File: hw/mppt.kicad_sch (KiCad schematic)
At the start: 9 parts

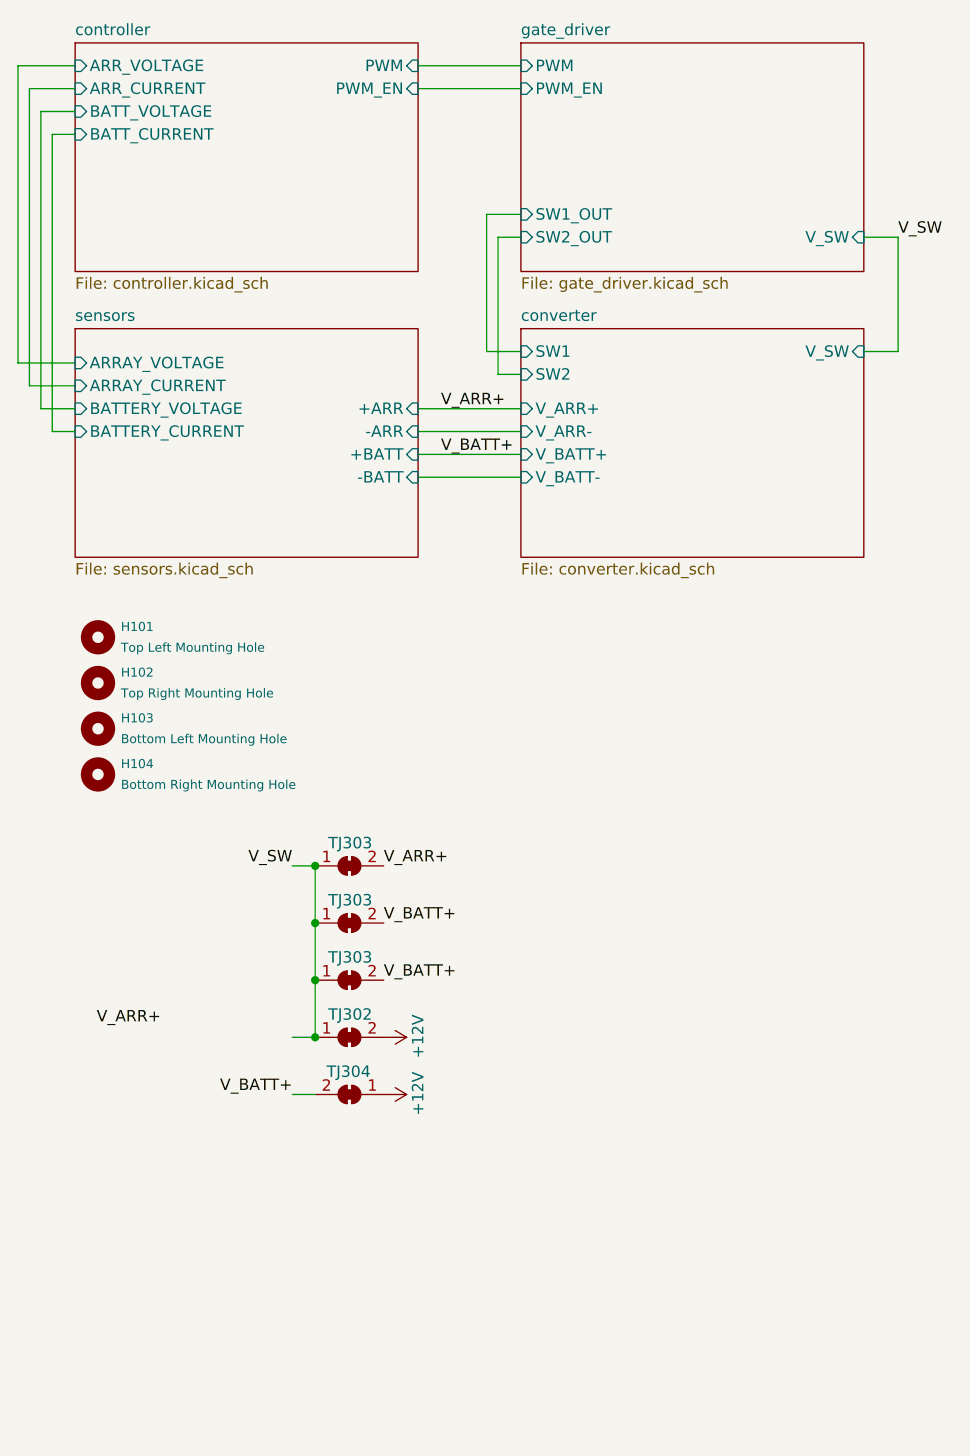
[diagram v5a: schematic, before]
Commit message: Added proper signal TPs for Vsw, both gate signals, and PWM, added BNC connector for PWM control signal to STM analog pin, increased Vsw zone on F.cu, in.1, and in.2, reduced vias directly under fets, changed heatsink holesto pads for proper zone margins
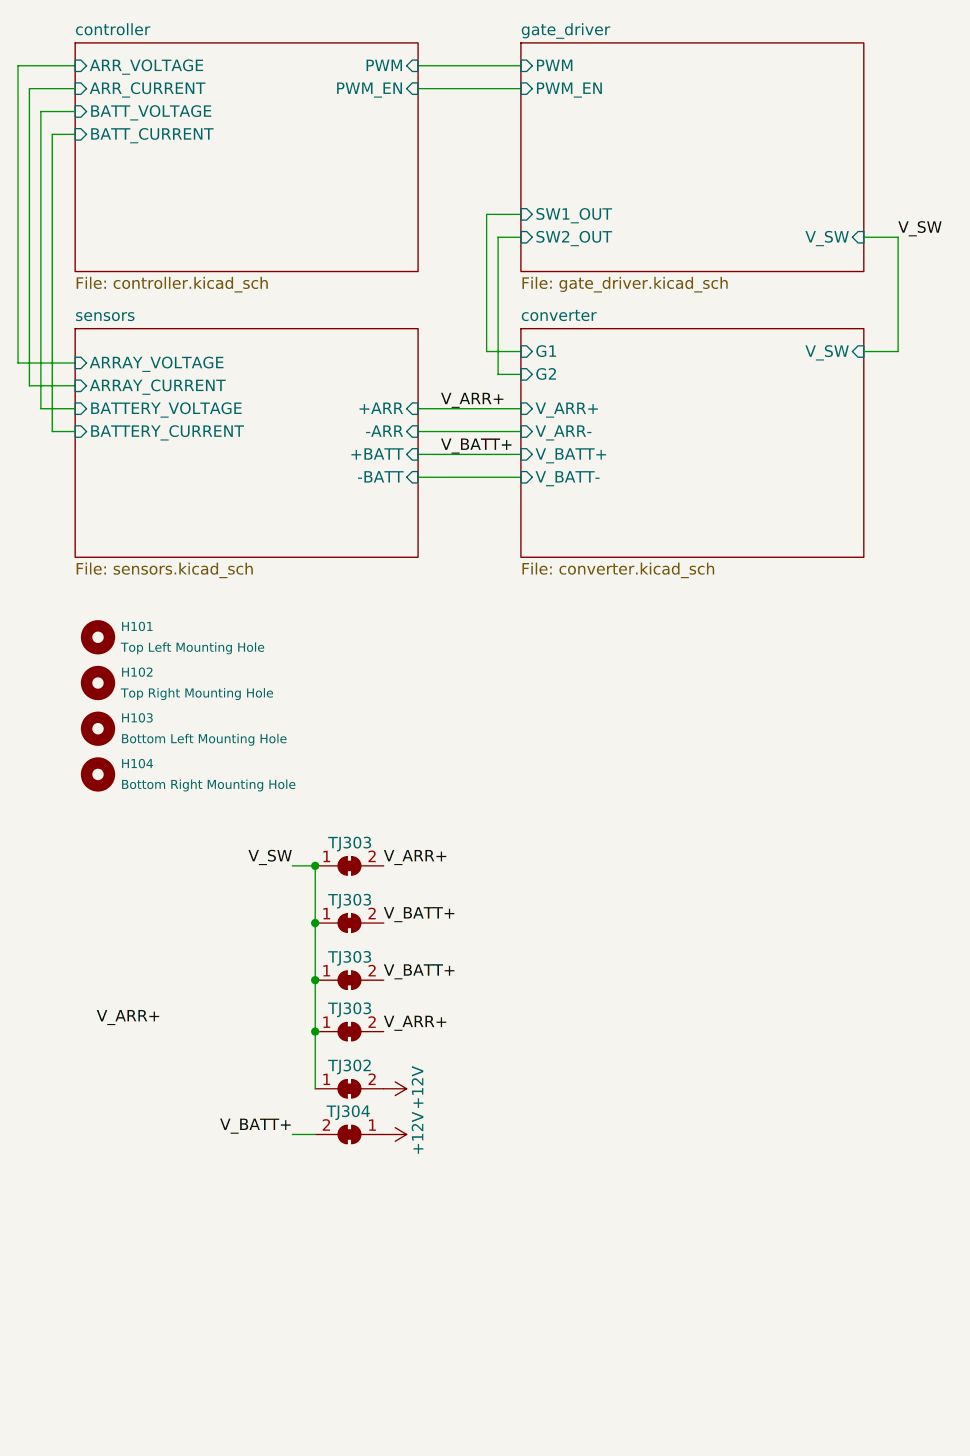
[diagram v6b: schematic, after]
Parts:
- added TJ303: Thermal Jumper, Resistor_SMD:R_0805_2012Metric, symbol Jumper:SolderJumper_2_Bridged
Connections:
- net V_ARR+: now also TJ303.2 (B)
- net V_SW: now also TJ303.1 (A)
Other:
- sheet converter ports: added G1, G2; removed SW1, SW2
- moved on the sheet: TJ302, TJ304
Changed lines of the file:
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@@
   (junction (at 60.96 133.35) (diameter 0) (color 0 0 0 0)
   )
-  (junction (at 60.96 146.05) (diameter 0) (color 0 0 0 0)
+  (junction (at 60.96 145.415) (diameter 0) (color 0 0 0 0)
   )
   (junction (at 60.96 127) (diameter 0) (color 0 0 0 0)
   )
-  (wire (pts (xy 60.96 139.7) (xy 60.96 146.05))
+  (wire (pts (xy 60.96 139.7) (xy 60.96 145.415))
     (stroke (width 0) (type default))
   )
@@
     (stroke (width 0) (type default))
   )
-  (wire (pts (xy 58.42 146.05) (xy 60.96 146.05))
-    (stroke (width 0) (type default))
-  )
   (wire (pts (xy 60.96 127) (xy 60.96 133.35))
     (stroke (width 0) (type default))
@@
     (stroke (width 0) (type default))
   )
+  (wire (pts (xy 60.96 145.415) (xy 60.96 151.765))
+    (stroke (width 0) (type default))
+  )
   (wire (pts (xy 31.75 45.72) (xy 31.75 78.74))
     (stroke (width 0) (type default))
@@
     (stroke (width 0) (type default))
   )
-  (wire (pts (xy 58.42 152.4) (xy 60.96 152.4))
+  (wire (pts (xy 58.42 156.845) (xy 60.96 156.845))
     (stroke (width 0) (type default))
   )
@@
   (wire (pts (xy 34.29 43.18) (xy 30.48 43.18))
     (stroke (width 0) (type default))
+  )
+  (label "V_ARR+" (at 68.58 145.415 0) (fields_autoplaced)
+    (effects (font (size 1.27 1.27)) (justify left bottom))
   )
   (label "V_BATT+" (at 68.58 139.7 0) (fields_autoplaced)
@@
     (effects (font (size 1.27 1.27)) (justify right bottom))
   )
-  (label "V_BATT+" (at 58.42 152.4 180) (fields_autoplaced)
+  (label "V_BATT+" (at 58.42 156.845 180) (fields_autoplaced)
     (effects (font (size 1.27 1.27)) (justify right bottom))
   )
@@
     (effects (font (size 1.27 1.27)) (justify left bottom))
   )
-  (symbol (lib_id "Jumper:SolderJumper_2_Bridged") (at 64.77 152.4 180) (unit 1)
-    (in_bom yes) (on_board yes) (dnp no)
-    (property "Reference" "TJ304" (at 62.23 149.86 0)
-      (effects (font (size 1.27 1.27)) (justify right))
-    )
-    (property "Value" "Thermal Jumper" (at 58.42 149.86 0)
+  (symbol (lib_id "Jumper:SolderJumper_2_Bridged") (at 64.77 156.845 180) (unit 1)
+    (in_bom yes) (on_board yes) (dnp no)
+    (property "Reference" "TJ304" (at 62.23 154.305 0)
+      (effects (font (size 1.27 1.27)) (justify right))
+    )
+    (property "Value" "Thermal Jumper" (at 58.42 154.305 0)
       (effects (font (size 1.27 1.27)) (justify right) hide)
     )
-    (property "Footprint" "Resistor_SMD:R_0805_2012Metric" (at 64.77 152.4 0)
-      (effects (font (size 1.27 1.27)) hide)
-    )
-    (property "Datasheet" "~" (at 64.77 152.4 0)
-      (effects (font (size 1.27 1.27)) hide)
-    )
-    (property "Mfr PN" "QB0805B40WYT" (at 64.77 152.4 0)
+    (property "Footprint" "Resistor_SMD:R_0805_2012Metric" (at 64.77 156.845 0)
+      (effects (font (size 1.27 1.27)) hide)
+    )
+    (property "Datasheet" "~" (at 64.77 156.845 0)
+      (effects (font (size 1.27 1.27)) hide)
+    )
+    (property "Mfr PN" "QB0805B40WYT" (at 64.77 156.845 0)
       (effects (font (size 1.27 1.27)) hide)
     )
@@
     )
   )
+  (symbol (lib_id "Jumper:SolderJumper_2_Bridged") (at 64.77 145.415 0) (unit 1)
+    (in_bom yes) (on_board yes) (dnp no)
+    (property "Reference" "TJ303" (at 67.31 142.875 0)
+      (effects (font (size 1.27 1.27)) (justify right))
+    )
+    (property "Value" "Thermal Jumper" (at 71.12 147.955 0)
+      (effects (font (size 1.27 1.27)) (justify right) hide)
+    )
+    (property "Footprint" "Resistor_SMD:R_0805_2012Metric" (at 64.77 145.415 0)
+      (effects (font (size 1.27 1.27)) hide)
+    )
+    (property "Datasheet" "~" (at 64.77 145.415 0)
+      (effects (font (size 1.27 1.27)) hide)
+    )
+    (property "Mfr PN" "QB0805B40WYT" (at 64.77 145.415 0)
+      (effects (font (size 1.27 1.27)) hide)
+    )
+    (pin "1")
+    (pin "2")
+    (instances
+      (project "mppt"
+        (path "/06fd3a42-664d-41bc-bf0f-b5ee0ddcc902/9cd55a57-0ec8-481d-b571-b5fdbe353ce7"
+          (reference "TJ303") (unit 1)
+        )
+        (path "/06fd3a42-664d-41bc-bf0f-b5ee0ddcc902"
+          (reference "TJ106") (unit 1)
+        )
+      )
+    )
+  )
   (symbol (lib_id "Mechanical:MountingHole") (at 36.83 106.68 0) (unit 1)
     (in_bom yes) (on_board yes) (dnp no)
@@
     )
   )
-  (symbol (lib_id "power:+12V") (at 68.58 146.05 270) (unit 1)
-    (in_bom yes) (on_board yes) (dnp no)
-    (property "Reference" "#PWR0101" (at 64.77 146.05 0)
-      (effects (font (size 1.27 1.27)) hide)
-    )
-    (property "Value" "+12V" (at 72.39 143.51 0)
-      (effects (font (size 1.27 1.27)) (justify left))
-    )
-    (property "Footprint" "" (at 68.58 146.05 0)
-      (effects (font (size 1.27 1.27)) hide)
-    )
-    (property "Datasheet" "" (at 68.58 146.05 0)
+  (symbol (lib_id "power:+12V") (at 68.58 151.765 270) (unit 1)
+    (in_bom yes) (on_board yes) (dnp no)
+    (property "Reference" "#PWR0101" (at 64.77 151.765 0)
+      (effects (font (size 1.27 1.27)) hide)
+    )
+    (property "Value" "+12V" (at 72.39 149.225 0)
+      (effects (font (size 1.27 1.27)) (justify left))
+    )
+    (property "Footprint" "" (at 68.58 151.765 0)
+      (effects (font (size 1.27 1.27)) hide)
+    )
+    (property "Datasheet" "" (at 68.58 151.765 0)
       (effects (font (size 1.27 1.27)) hide)
     )
@@
     )
   )
-  (symbol (lib_id "power:+12V") (at 68.58 152.4 270) (unit 1)
-    (in_bom yes) (on_board yes) (dnp no)
-    (property "Reference" "#PWR0102" (at 64.77 152.4 0)
-      (effects (font (size 1.27 1.27)) hide)
-    )
-    (property "Value" "+12V" (at 72.39 149.86 0)
-      (effects (font (size 1.27 1.27)) (justify left))
-    )
-    (property "Footprint" "" (at 68.58 152.4 0)
-      (effects (font (size 1.27 1.27)) hide)
-    )
-    (property "Datasheet" "" (at 68.58 152.4 0)
+  (symbol (lib_id "power:+12V") (at 68.58 156.845 270) (unit 1)
+    (in_bom yes) (on_board yes) (dnp no)
+    (property "Reference" "#PWR0102" (at 64.77 156.845 0)
+      (effects (font (size 1.27 1.27)) hide)
+    )
+    (property "Value" "+12V" (at 72.39 154.305 0)
+      (effects (font (size 1.27 1.27)) (justify left))
+    )
+    (property "Footprint" "" (at 68.58 156.845 0)
+      (effects (font (size 1.27 1.27)) hide)
+    )
+    (property "Datasheet" "" (at 68.58 156.845 0)
       (effects (font (size 1.27 1.27)) hide)
     )
@@
     )
   )
-  (symbol (lib_id "Jumper:SolderJumper_2_Bridged") (at 64.77 146.05 0) (unit 1)
-    (in_bom yes) (on_board yes) (dnp no)
-    (property "Reference" "TJ302" (at 67.31 143.51 0)
-      (effects (font (size 1.27 1.27)) (justify right))
-    )
-    (property "Value" "Thermal Jumper" (at 71.12 148.59 0)
+  (symbol (lib_id "Jumper:SolderJumper_2_Bridged") (at 64.77 151.765 0) (unit 1)
+    (in_bom yes) (on_board yes) (dnp no)
+    (property "Reference" "TJ302" (at 67.31 149.225 0)
+      (effects (font (size 1.27 1.27)) (justify right))
+    )
+    (property "Value" "Thermal Jumper" (at 71.12 154.305 0)
       (effects (font (size 1.27 1.27)) (justify right) hide)
     )
-    (property "Footprint" "Resistor_SMD:R_0805_2012Metric" (at 64.77 146.05 0)
-      (effects (font (size 1.27 1.27)) hide)
-    )
-    (property "Datasheet" "~" (at 64.77 146.05 0)
-      (effects (font (size 1.27 1.27)) hide)
-    )
-    (property "Mfr PN" "QB0805B40WYT" (at 64.77 146.05 0)
+    (property "Footprint" "Resistor_SMD:R_0805_2012Metric" (at 64.77 151.765 0)
+      (effects (font (size 1.27 1.27)) hide)
+    )
+    (property "Datasheet" "~" (at 64.77 151.765 0)
+      (effects (font (size 1.27 1.27)) hide)
+    )
+    (property "Mfr PN" "QB0805B40WYT" (at 64.77 151.765 0)
       (effects (font (size 1.27 1.27)) hide)
     )
@@
       (effects (font (size 1.27 1.27)) (justify left top))
     )
-    (pin "SW1" input (at 83.82 69.85 180)
-      (effects (font (size 1.27 1.27)) (justify left))
-    )
-    (pin "SW2" input (at 83.82 72.39 180)
-      (effects (font (size 1.27 1.27)) (justify left))
-    )
+    (pin "G1" input (at 83.82 69.85 180)
+      (effects (font (size 1.27 1.27)) (justify left))
+    )
+    (pin "G2" input (at 83.82 72.39 180)
+      (effects (font (size 1.27 1.27)) (justify left))
+    )
